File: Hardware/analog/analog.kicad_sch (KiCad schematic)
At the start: 0 parts

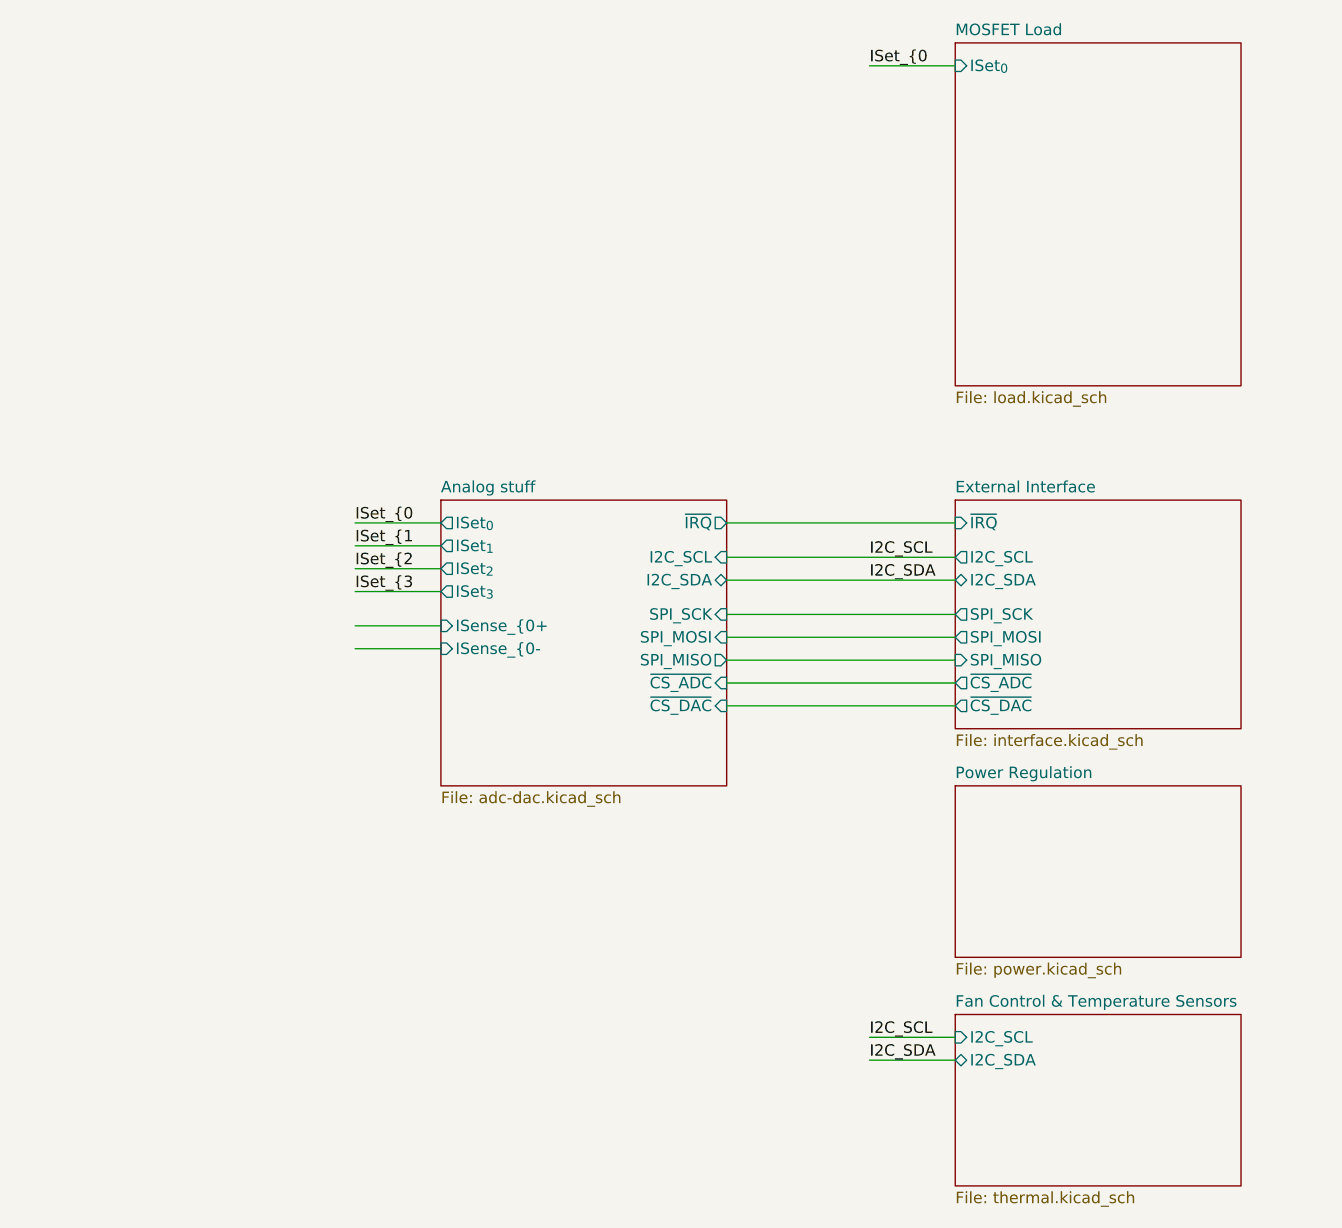
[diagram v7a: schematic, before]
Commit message: Initial pass at analog board
- Everything currently in the schematic is routed, and stuff is
  reasonably sanely laid out

- Some compromises: namely, the zero offset doesn't use the DAC
  reference for its positive, but generates a separate 2.5V via the
  shunt diodes; this is then shared between both op-amps. That avoids
  the DAC/ADC reference getting noisified

  Also, we don't have an ADC for measuring the temperature sensors yet,
  and in fact, those aren't routed out (or existent really) yet either

- TODO: add test points for drive voltages and current sense voltages
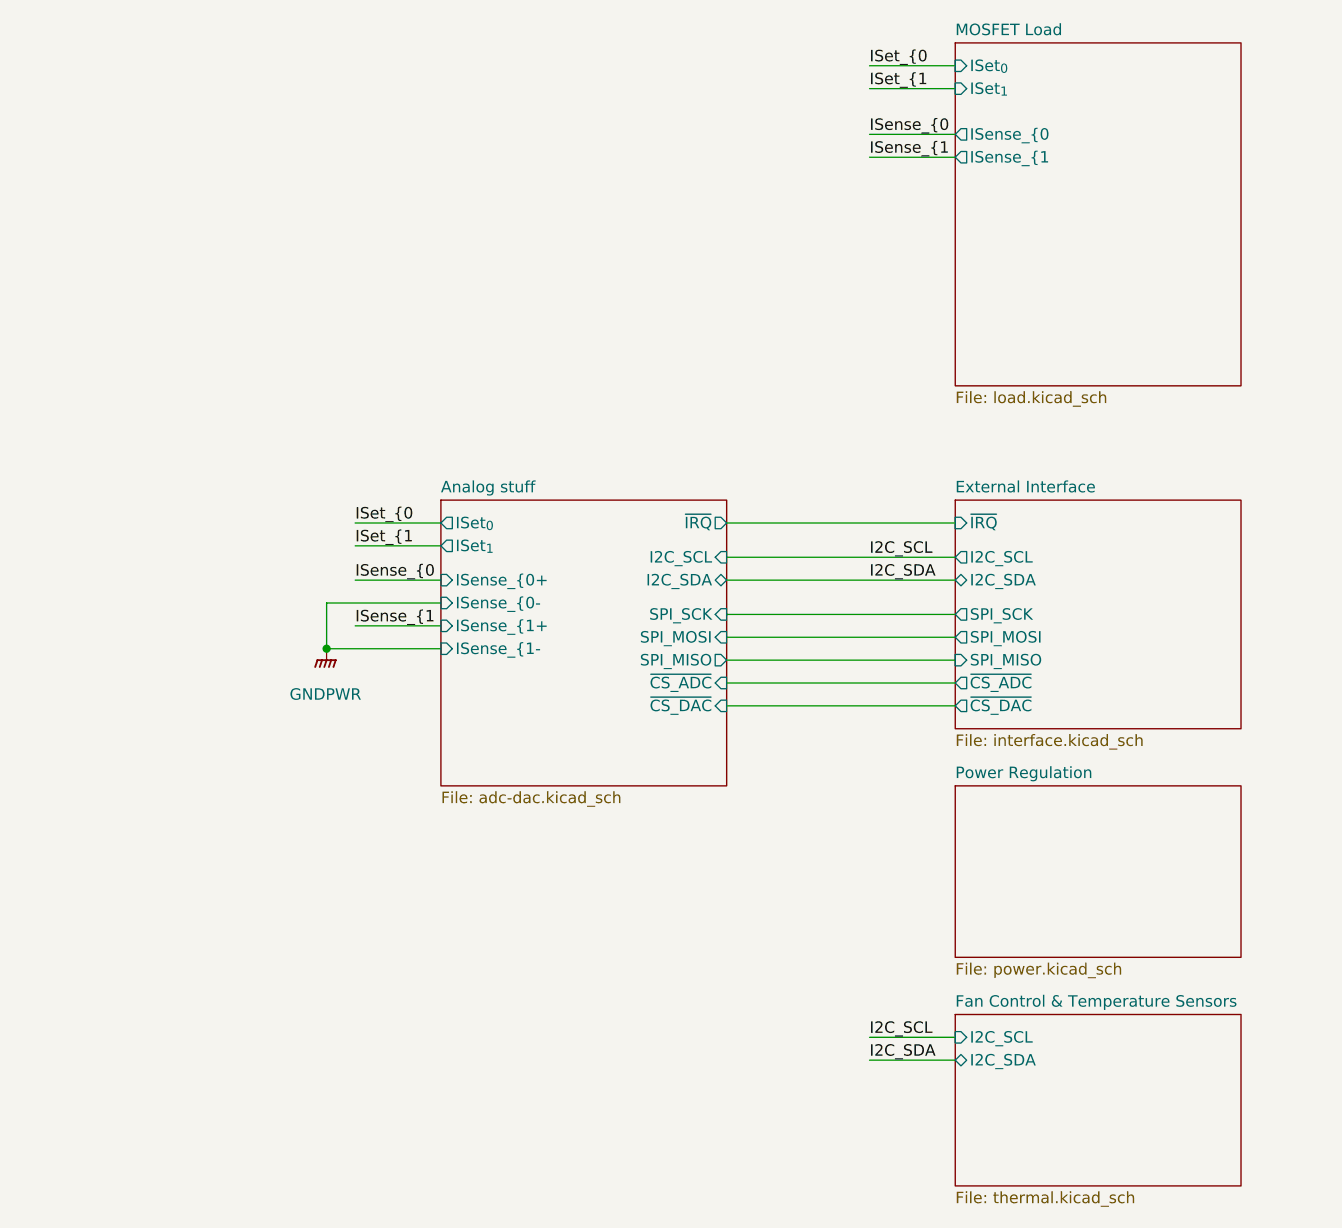
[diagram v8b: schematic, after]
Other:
- sheet Analog stuff ports: added ISense_{1+, ISense_{1-; removed ISet_{2}, ISet_{3}
- sheet MOSFET Load ports: added ISense_{0, ISense_{1, ISet_{1}; removed none
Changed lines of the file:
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@@
     (rev "1")
   )
+  (junction (at 158.75 92.71) (diameter 0) (color 0 0 0 0)
+  )
+  (wire (pts (xy 219.075 35.56) (xy 228.6 35.56))
+    (stroke (width 0) (type default) (color 0 0 0 0))
+  )
+  (wire (pts (xy 219.075 30.48) (xy 228.6 30.48))
+    (stroke (width 0) (type default) (color 0 0 0 0))
+  )
   (wire (pts (xy 203.2 85.09) (xy 228.6 85.09))
     (stroke (width 0) (type default) (color 0 0 0 0))
@@
     (stroke (width 0) (type default) (color 0 0 0 0))
   )
-  (wire (pts (xy 161.925 86.36) (xy 171.45 86.36))
+  (wire (pts (xy 219.075 38.1) (xy 228.6 38.1))
     (stroke (width 0) (type default) (color 0 0 0 0))
   )
@@
     (stroke (width 0) (type default) (color 0 0 0 0))
   )
+  (wire (pts (xy 161.925 85.09) (xy 171.45 85.09))
+    (stroke (width 0) (type default) (color 0 0 0 0))
+  )
+  (wire (pts (xy 158.75 92.71) (xy 171.45 92.71))
+    (stroke (width 0) (type default) (color 0 0 0 0))
+  )
+  (wire (pts (xy 161.925 81.28) (xy 171.45 81.28))
+    (stroke (width 0) (type default) (color 0 0 0 0))
+  )
+  (wire (pts (xy 203.2 96.52) (xy 228.6 96.52))
+    (stroke (width 0) (type default) (color 0 0 0 0))
+  )
+  (wire (pts (xy 203.2 78.74) (xy 228.6 78.74))
+    (stroke (width 0) (type default) (color 0 0 0 0))
+  )
+  (wire (pts (xy 158.75 92.71) (xy 158.75 87.63))
+    (stroke (width 0) (type default) (color 0 0 0 0))
+  )
   (wire (pts (xy 161.925 90.17) (xy 171.45 90.17))
     (stroke (width 0) (type default) (color 0 0 0 0))
   )
-  (wire (pts (xy 161.925 81.28) (xy 171.45 81.28))
-    (stroke (width 0) (type default) (color 0 0 0 0))
-  )
-  (wire (pts (xy 203.2 96.52) (xy 228.6 96.52))
-    (stroke (width 0) (type default) (color 0 0 0 0))
-  )
-  (wire (pts (xy 203.2 78.74) (xy 228.6 78.74))
-    (stroke (width 0) (type default) (color 0 0 0 0))
-  )
-  (wire (pts (xy 161.925 83.82) (xy 171.45 83.82))
-    (stroke (width 0) (type default) (color 0 0 0 0))
-  )
-  (wire (pts (xy 161.925 92.71) (xy 171.45 92.71))
+  (wire (pts (xy 158.75 87.63) (xy 171.45 87.63))
     (stroke (width 0) (type default) (color 0 0 0 0))
   )
@@
     (stroke (width 0) (type default) (color 0 0 0 0))
   )
+  (label "ISense_{0" (at 219.075 35.56 0)
+    (effects (font (size 1.27 1.27)) (justify left bottom))
+  )
   (label "I2C_SDA" (at 219.075 85.09 0)
     (effects (font (size 1.27 1.27)) (justify left bottom))
@@
     (effects (font (size 1.27 1.27)) (justify left bottom))
   )
-  (label "ISet_{2" (at 161.925 83.82 0)
+  (label "ISense_{1" (at 161.925 90.17 0)
+    (effects (font (size 1.27 1.27)) (justify left bottom))
+  )
+  (label "ISense_{1" (at 219.075 38.1 0)
     (effects (font (size 1.27 1.27)) (justify left bottom))
   )
@@
     (effects (font (size 1.27 1.27)) (justify left bottom))
   )
+  (label "ISet_{1" (at 219.075 30.48 0)
+    (effects (font (size 1.27 1.27)) (justify left bottom))
+  )
   (label "ISet_{1" (at 161.925 81.28 0)
     (effects (font (size 1.27 1.27)) (justify left bottom))
@@
     (effects (font (size 1.27 1.27)) (justify left bottom))
   )
-  (label "ISet_{3" (at 161.925 86.36 0)
-    (effects (font (size 1.27 1.27)) (justify left bottom))
-  )
   (label "ISet_{0" (at 219.075 27.94 0)
     (effects (font (size 1.27 1.27)) (justify left bottom))
   )
+  (label "ISense_{0" (at 161.925 85.09 0)
+    (effects (font (size 1.27 1.27)) (justify left bottom))
+  )
   (label "I2C_SCL" (at 219.075 82.55 0)
     (effects (font (size 1.27 1.27)) (justify left bottom))
+  )
+  (symbol (lib_id "power:GNDPWR") (at 158.75 92.71 0) (unit 1)
+    (in_bom yes) (on_board yes) (fields_autoplaced)
+    (property "Reference" "#PWR0122" (id 0) (at 158.75 97.79 0)
+      (effects (font (size 1.27 1.27)) hide)
+    )
+    (property "Value" "GNDPWR" (id 1) (at 158.623 97.79 0))
+    (property "Footprint" "" (id 2) (at 158.75 93.98 0)
+      (effects (font (size 1.27 1.27)) hide)
+    )
+    (property "Datasheet" "" (id 3) (at 158.75 93.98 0)
+      (effects (font (size 1.27 1.27)) hide)
+    )
+    (pin "1")
   )
   (sheet (at 228.6 107.95) (size 31.75 19.05) (fields_autoplaced)
@@
       (effects (font (size 1.27 1.27)) (justify left))
     )
-    (pin "ISet_{2}" output (at 171.45 83.82 180)
-      (effects (font (size 1.27 1.27)) (justify left))
-    )
-    (pin "ISet_{3}" output (at 171.45 86.36 180)
-      (effects (font (size 1.27 1.27)) (justify left))
-    )
-    (pin "ISense_{0+" input (at 171.45 90.17 180)
-      (effects (font (size 1.27 1.27)) (justify left))
-    )
-    (pin "ISense_{0-" input (at 171.45 92.71 180)
+    (pin "ISense_{0+" input (at 171.45 85.09 180)
+      (effects (font (size 1.27 1.27)) (justify left))
+    )
+    (pin "ISense_{0-" input (at 171.45 87.63 180)
+      (effects (font (size 1.27 1.27)) (justify left))
+    )
+    (pin "ISense_{1+" input (at 171.45 90.17 180)
+      (effects (font (size 1.27 1.27)) (justify left))
+    )
+    (pin "ISense_{1-" input (at 171.45 92.71 180)
       (effects (font (size 1.27 1.27)) (justify left))
     )
@@
     )
     (pin "ISet_{0}" input (at 228.6 27.94 180)
+      (effects (font (size 1.27 1.27)) (justify left))
+    )
+    (pin "ISet_{1}" input (at 228.6 30.48 180)
+      (effects (font (size 1.27 1.27)) (justify left))
+    )
+    (pin "ISense_{1" output (at 228.6 38.1 180)
+      (effects (font (size 1.27 1.27)) (justify left))
+    )
+    (pin "ISense_{0" output (at 228.6 35.56 180)
       (effects (font (size 1.27 1.27)) (justify left))
     )
@@
       (reference "#PWR0120") (unit 1) (value "GNDA") (footprint "")
     )
+    (path "/a6dcbea5-6bb6-4f0f-ad38-0b8287d8346c/5669583d-b1ba-412f-a93d-0ab40bfc48a5"
+      (reference "#PWR0121") (unit 1) (value "GND") (footprint "")
+    )
+    (path "/cf068d0d-8ab8-4c03-a894-9ed9780c90b8"
+      (reference "#PWR0122") (unit 1) (value "GNDPWR") (footprint "")
+    )
+    (path "/e1649c35-e6e3-47dd-8aeb-a217676fe0ce/fd3f89b3-e019-4626-ab8f-e770de9803d3"
+      (reference "#PWR0123") (unit 1) (value "GND") (footprint "")
+    )
     (path "/e1649c35-e6e3-47dd-8aeb-a217676fe0ce/d6b232d9-faf0-4a9d-8350-e9a8056ff3c8"
       (reference "#PWR0201") (unit 1) (value "GNDPWR") (footprint "")
@@
       (reference "#PWR0215") (unit 1) (value "GND") (footprint "")
     )
-    (path "/e1649c35-e6e3-47dd-8aeb-a217676fe0ce/5629f661-91ba-4482-92f9-563bc43b0660"
-      (reference "#PWR0216") (unit 1) (value "-5VA") (footprint "")
-    )
-    (path "/e1649c35-e6e3-47dd-8aeb-a217676fe0ce/fc892e26-c3db-40cc-a8e8-335d5f7f739b"
-      (reference "#PWR0217") (unit 1) (value "GND") (footprint "")
+    (path "/e1649c35-e6e3-47dd-8aeb-a217676fe0ce/4483b914-ee1e-412b-9677-33504e4ebc91"
+      (reference "#PWR0216") (unit 1) (value "+5VA") (footprint "")
     )
     (path "/b8f9c5f7-2403-4b47-9202-13f82aeee8e6/d8bd1851-6f6f-4be1-a9cc-5f8b88bf9564"
@@
       (reference "#PWR0613") (unit 1) (value "GNDA") (footprint "")
     )
-    (path "/a6dcbea5-6bb6-4f0f-ad38-0b8287d8346c/5669583d-b1ba-412f-a93d-0ab40bfc48a5"
-      (reference "#PWR?") (unit 1) (value "GND") (footprint "")
-    )
     (path "/e1649c35-e6e3-47dd-8aeb-a217676fe0ce/82c2c0cf-1141-4c1a-8013-130daf3cd355"
       (reference "C201") (unit 1) (value "1nF") (footprint "Capacitor_SMD:C_0805_2012Metric_Pad1.18x1.45mm_HandSolder")
@@
       (reference "C204") (unit 1) (value "22nF") (footprint "Capacitor_SMD:C_0805_2012Metric_Pad1.18x1.45mm_HandSolder")
     )
+    (path "/e1649c35-e6e3-47dd-8aeb-a217676fe0ce/d8ada413-0b8b-44b4-81a0-521278e35bb3"
+      (reference "C205") (unit 1) (value "100nF") (footprint "Capacitor_SMD:C_0805_2012Metric_Pad1.18x1.45mm_HandSolder")
+    )
+    (path "/e1649c35-e6e3-47dd-8aeb-a217676fe0ce/8188f1c2-dd3f-42cb-87a9-f529e62f6ff7"
+      (reference "C206") (unit 1) (value "100nF") (footprint "Capacitor_SMD:C_0805_2012Metric_Pad1.18x1.45mm_HandSolder")
+    )
     (path "/b8f9c5f7-2403-4b47-9202-13f82aeee8e6/94dcf60e-17f7-44b3-8cfb-6ab8614294f5"
       (reference "C301") (unit 1) (value "47µF") (footprint "Capacitor_THT:CP_Radial_D6.3mm_P2.50mm")
@@
       (reference "R213") (unit 1) (value "330k (?)") (footprint "Resistor_SMD:R_0805_2012Metric_Pad1.20x1.40mm_HandSolder")
     )
-    (path "/e1649c35-e6e3-47dd-8aeb-a217676fe0ce/7a6711de-78ab-4b0f-bdab-ebe78c68428e"
+    (path "/e1649c35-e6e3-47dd-8aeb-a217676fe0ce/c7cd4e43-1364-4d3e-932a-d8e98df8ac24"
       (reference "R214") (unit 1) (value "1k") (footprint "Resistor_SMD:R_0805_2012Metric_Pad1.20x1.40mm_HandSolder")
     )
@@
       (reference "U204") (unit 3) (value "ADA4522-2") (footprint "Package_SO:SOIC-8_3.9x4.9mm_P1.27mm")
     )
-    (path "/e1649c35-e6e3-47dd-8aeb-a217676fe0ce/57e5048c-5c2b-4e2e-a31f-94b551c43df9"
+    (path "/e1649c35-e6e3-47dd-8aeb-a217676fe0ce/58094694-4489-4c34-bc51-b0a855ddabad"
       (reference "U205") (unit 1) (value "LM431SC") (footprint "Package_TO_SOT_SMD:SOT-23")
     )
